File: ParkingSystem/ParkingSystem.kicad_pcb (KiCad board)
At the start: 2 copper layers, 55.9 x 64.1 mm, 45 parts, among them J1 PJ-002A, J2 0430450400, J3 Conn_ARM_JTAG_SWD_10, J4 Conn_01x04_Female, J5 0430450200, Q1 SSM3K333R,LF, Q2 SSM3K333R,LF, Q3 SSM3K333R,LF, Q4 SSM3K333R,LF, Q5 SSM3K333R,LF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

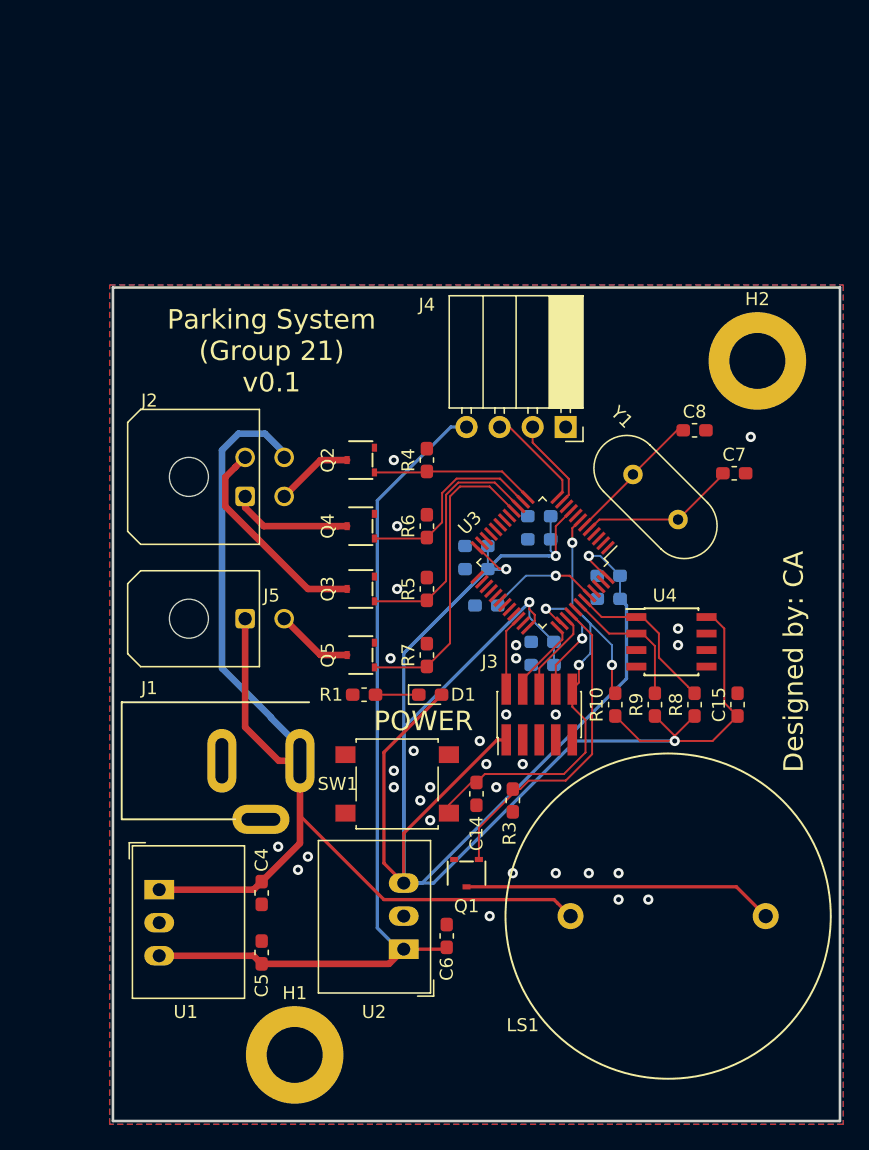
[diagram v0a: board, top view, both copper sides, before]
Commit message: Create sn74L47 footprint and begin pcb layout
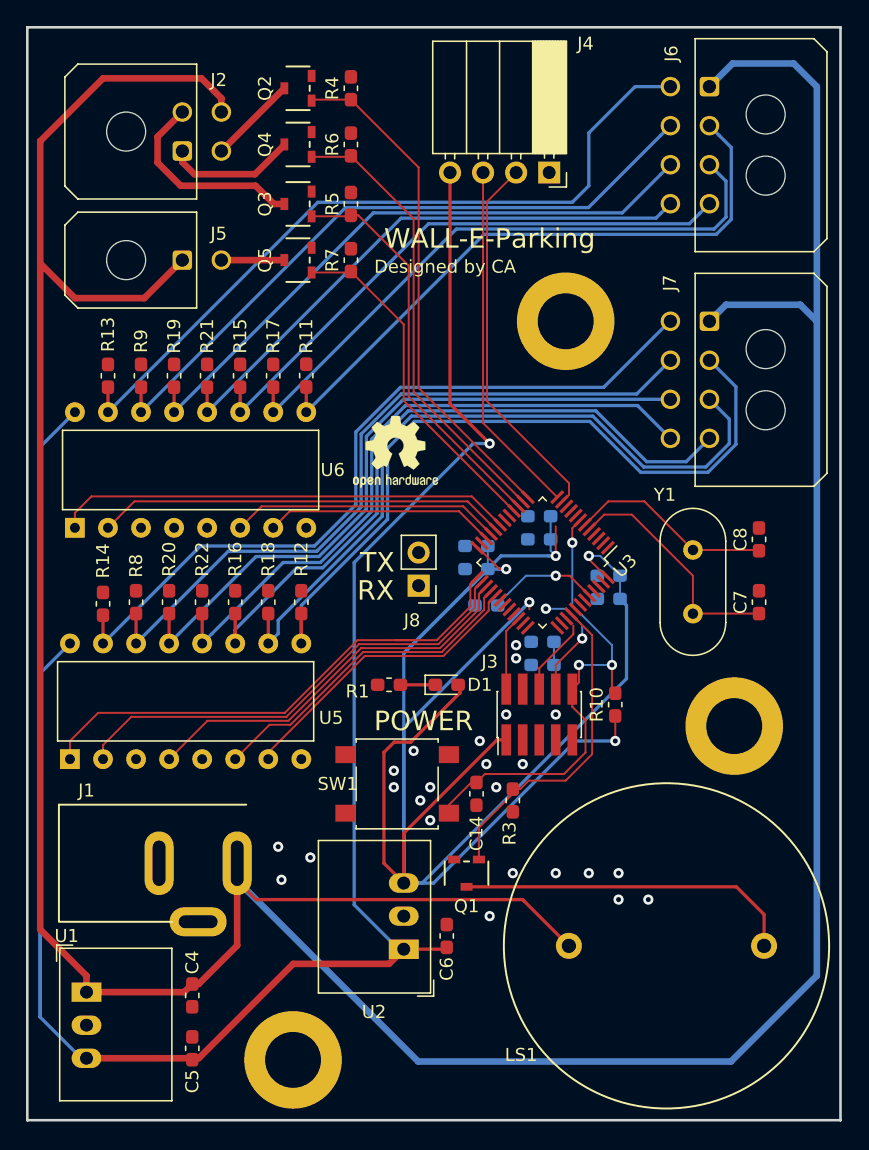
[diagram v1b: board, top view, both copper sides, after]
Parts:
- removed C15: 0u1, Capacitor_SMD:C_0603_1608Metric_Pad1.05x0.95mm_HandSolder
- removed U4: DS1621S, Package_SO:SOIC-8_3.9x4.9mm_P1.27mm
- added ?: OSHW-Logo2_7.3x6mm_SilkScreen, Symbol:OSHW-Logo2_7.3x6mm_SilkScreen, F.Cu at (90.3, 47.6)
- added H3: MountingHole, MountingHole:MountingHole_4.3mm_M4_DIN965_Pad, F.Cu at (103.4, 37.6)
- added J6: Conn_01x08_Female, Connector_Molex:Molex_Micro-Fit_3.0_43045-0800_2x04_P3.00mm_Horizontal, F.Cu at (114.4, 19.6)
- added J7: Conn_01x08_Female, Connector_Molex:Molex_Micro-Fit_3.0_43045-0800_2x04_P3.00mm_Horizontal, F.Cu at (114.4, 37.6)
- added J8: Conn_01x02_Female, Connector_PinHeader_2.54mm:PinHeader_1x02_P2.54mm_Vertical, F.Cu at (92.1, 57.9)
- added R11: 1K, Resistor_SMD:R_0603_1608Metric_Pad1.05x0.95mm_HandSolder, F.Cu at (83.4, 41.8)
- added R12: 1K, Resistor_SMD:R_0603_1608Metric_Pad1.05x0.95mm_HandSolder, F.Cu at (83.1, 59.2)
- added R13: 1K, Resistor_SMD:R_0603_1608Metric_Pad1.05x0.95mm_HandSolder, F.Cu at (68.2, 41.8)
- added R14: 1K, Resistor_SMD:R_0603_1608Metric_Pad1.05x0.95mm_HandSolder, F.Cu at (67.8, 59.3)
- added R15: 1K, Resistor_SMD:R_0603_1608Metric_Pad1.05x0.95mm_HandSolder, F.Cu at (78.4, 41.8)
- added R16: 1K, Resistor_SMD:R_0603_1608Metric_Pad1.05x0.95mm_HandSolder, F.Cu at (78.0, 59.2)
- added R17: 1K, Resistor_SMD:R_0603_1608Metric_Pad1.05x0.95mm_HandSolder, F.Cu at (80.9, 41.8)
- added R18: 1K, Resistor_SMD:R_0603_1608Metric_Pad1.05x0.95mm_HandSolder, F.Cu at (80.5, 59.2)
- added R19: 1K, Resistor_SMD:R_0603_1608Metric_Pad1.05x0.95mm_HandSolder, F.Cu at (73.3, 41.8)
- added R20: 1K, Resistor_SMD:R_0603_1608Metric_Pad1.05x0.95mm_HandSolder, F.Cu at (72.9, 59.2)
- added R21: 1K, Resistor_SMD:R_0603_1608Metric_Pad1.05x0.95mm_HandSolder, F.Cu at (75.8, 41.8)
- added R22: 1K, Resistor_SMD:R_0603_1608Metric_Pad1.05x0.95mm_HandSolder, F.Cu at (75.4, 59.2)
- added U5: 74LS47, Drivers:SN74LS47N, F.Cu at (74.2, 66.8)
- added U6: 74LS47, Drivers:SN74LS47N, F.Cu at (74.5, 49.0)
- C14: value 0u1 -> 100n
- R8, R9: value 4k7 -> 1K
- moved R9 46.9 mm to (70.7, 41.8)
- moved R8 43.6 mm to (70.4, 59.2)
- moved R7 30.9 mm to (86.9, 32.9)
- moved Q5 30.7 mm to (82.8, 32.9)
- moved R5 30.2 mm to (86.9, 28.6)
- moved Q3 30.0 mm to (82.8, 28.6)
- moved R6 29.9 mm to (86.9, 24.0)
- moved Q4 29.7 mm to (82.8, 24.0)
- moved R4 29.2 mm to (86.9, 19.7)
- moved Q2 29.0 mm to (82.8, 19.7)
- moved H2 28.1 mm to (116.3, 68.7)
- moved J5 28.0 mm to (73.9, 32.9)
- moved J2 27.0 mm to (73.9, 24.5)
- moved J4 19.6 mm to (102.1, 26.2)
- moved C7 10.1 mm to (118.2, 59.2), turned to 90 degrees
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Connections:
- J1 pad 2: Net-(J1-Pad2) -> GND
- R8 pad 1: +3V3 -> /D1_g
- R8 pad 2: /I2C1_SDA -> +12V
- R9 pad 1: +3V3 -> /D0_g
- R9 pad 2: /I2C1_SCL -> +12V
- U3 pad 19: Net-(U3-Pad19) -> /S0_B
- U3 pad 20: Net-(U3-Pad20) -> /S0_C
- U3 pad 21: Net-(U3-Pad21) -> /S0_D
- U3 pad 22: Net-(U3-Pad22) -> /S0_A
- U3 pad 25: Net-(U3-Pad25) -> /S1_B
- U3 pad 26: Net-(U3-Pad26) -> /S1_C
- U3 pad 27: Net-(U3-Pad27) -> /BI
- U3 pad 28: Net-(U3-Pad28) -> /S1_D
- U3 pad 29: Net-(U3-Pad29) -> /S1_A
- U3 pad 30: Net-(U3-Pad30) -> /USART_TX
- U3 pad 31: Net-(U3-Pad31) -> /USART_RX
- U3 pad 42: /I2C1_SCL -> Net-(U3-Pad42)
- U3 pad 43: /I2C1_SDA -> Net-(U3-Pad43)
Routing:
- net +12V: track 93.1 -> 287.8 mm
- net +5V: track 67.6 -> 181.2 mm, vias 0 -> 1
- net /D1_f: track 0.00 -> 59.3 mm
- net /D0_f: track 0.00 -> 57.9 mm
- net /D1_e: track 0.00 -> 57.5 mm
- net /D1_d: track 0.00 -> 55.8 mm
- net /D1_g: track 0.00 -> 55.7 mm
- net /D1_c: track 0.00 -> 52.4 mm
- net /D1_a: track 0.00 -> 51.9 mm
- net /D0_g: track 0.00 -> 51.7 mm
- net /D1_b: track 0.00 -> 50.2 mm
- net /D0_e: track 0.00 -> 48.6 mm
- net /D0_a: track 0.00 -> 47.9 mm
- net /D0_d: track 0.00 -> 47.5 mm
- net /D0_c: track 0.00 -> 44.6 mm
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- removed copper zone on B.Cu, net GND
- removed copper zone on F.Cu, net GND
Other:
- board size 55.9 x 64.1 mm -> 62.5 x 84 mm
- board text added: "Designed by CA"
- board text added: "RX"
- board text added: "TX"
- board text added: "WALL-E-Parking"
- board text removed: "Designed by: CA"
- board text removed: "Parking System (Group 21) v0.1"

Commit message: Add zones
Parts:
- R2: moved to F.Cu
- moved R2 11.3 mm to (108.5, 61.2), turned to 90 degrees
- moved J8 5.43 mm to (94.0, 63.0), turned to 135 degrees
- moved D1 5.22 mm to (89.0, 66.0)
- moved R1 1.56 mm to (88.9, 64.3), turned to 0 degrees
- moved R14 0.13 mm to (67.8, 59.2)
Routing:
- net +12V: track 287.8 -> 332.2 mm
- net /BI: track 30.6 -> 53.1 mm
- net /USART_RX: track 0.00 -> 7.31 mm
- net /SWDCLK: track 0.77 -> 6.58 mm
- net +3V3: track 174.8 -> 169.0 mm
- net Net-(R2-Pad2): track 8.70 -> 3.94 mm, vias 1 -> 0
- net /USART_TX: track 0.00 -> 3.47 mm
- net /S1_B: track 40.4 -> 37.1 mm, vias 1 -> 0
- net /TDI: track 9.07 -> 10.8 mm
- net /S0_B: track 35.3 -> 36.5 mm
- net /S0_C: track 31.5 -> 32.7 mm
- net /S0_D: track 20.8 -> 21.9 mm
- net /S0_A: track 17.8 -> 18.7 mm
- net Net-(D1-Pad1): track 2.68 -> 1.84 mm
- net /S1_C: track 36.2 -> 35.4 mm
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- added copper zone on B.Cu, net GND
- added copper zone on F.Cu, net GND
